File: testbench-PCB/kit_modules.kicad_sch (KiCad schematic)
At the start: 7 parts, among them U2 Rotary_encoder_switch_module, U3 Thermistor_module, U4 Relay_module, U6 Matrix_keyboard, U7 RTC_EEPROM_module

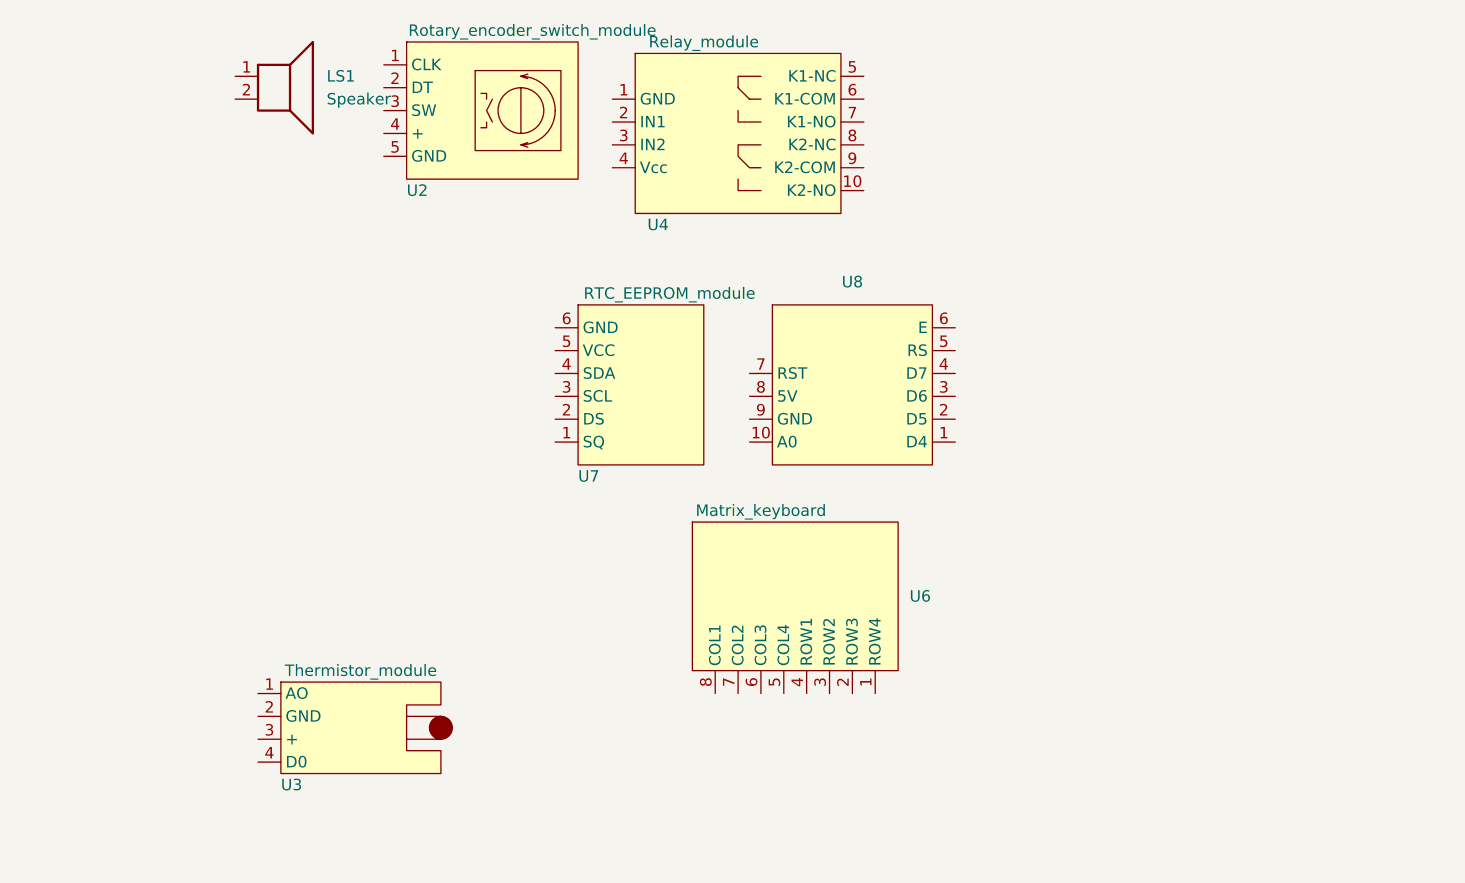
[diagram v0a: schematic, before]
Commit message: Changed USB interface name, MCU moved to separate sheet.
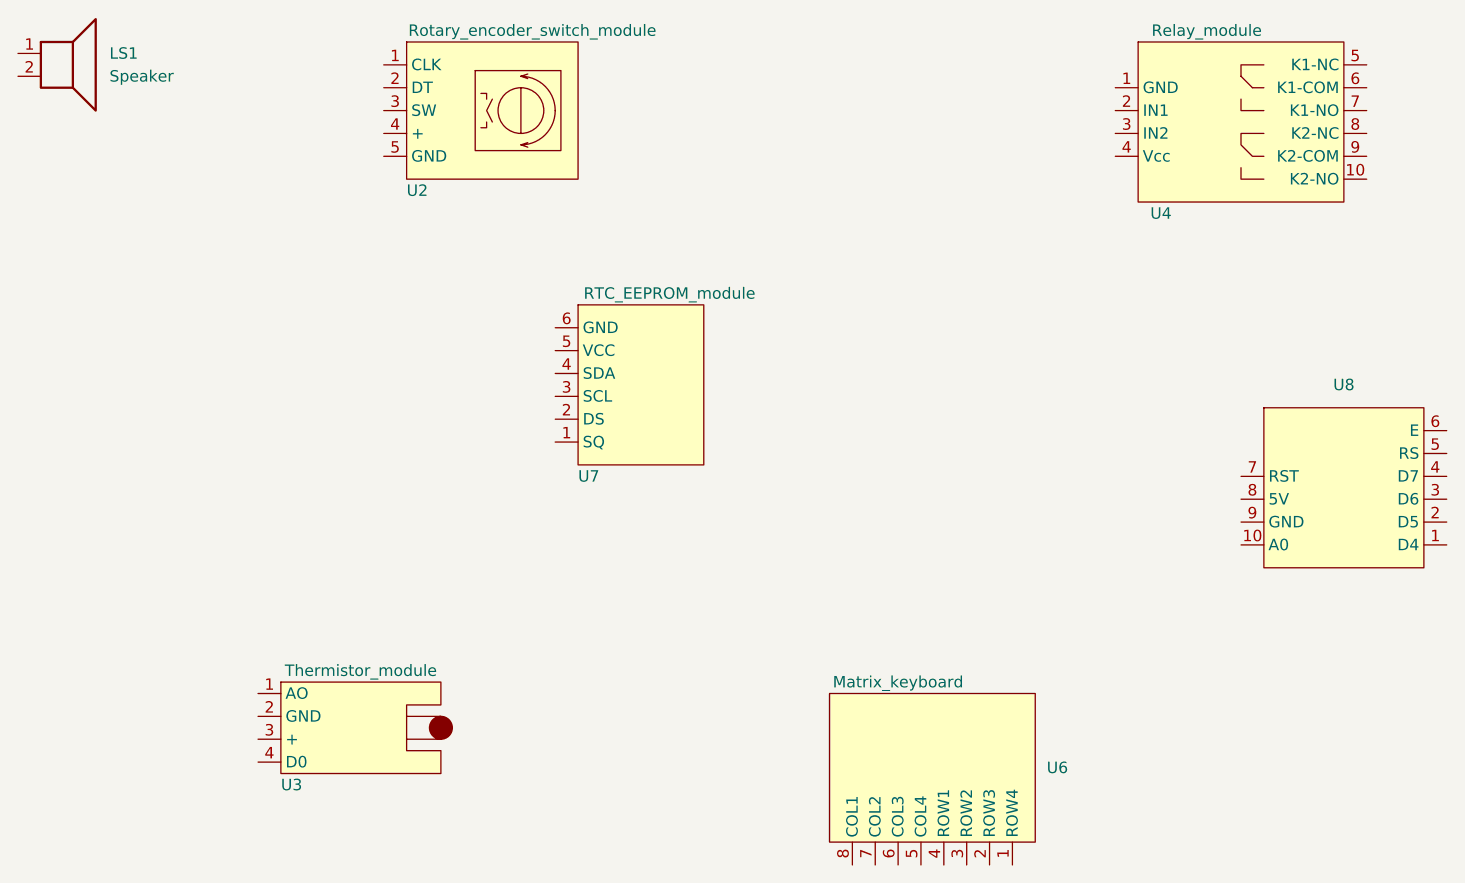
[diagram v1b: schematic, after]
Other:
- moved on the sheet: LS1, U4, U6, U8
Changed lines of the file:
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@@
 (kicad_sch (version 20230121) (generator eeschema)
   (paper "A4")
-  (symbol (lib_id "kit_modules:relay_module") (at 148.59 49.53 0) (unit 1)
-    (in_bom yes) (on_board yes) (dnp no)
-    (property "Reference" "U4" (at 153.67 59.69 0)
-      (effects (font (size 1.27 1.27)))
-    )
-    (property "Value" "Relay_module" (at 158.75 39.37 0)
-      (effects (font (size 1.27 1.27)))
-    )
-    (property "Footprint" "" (at 148.59 53.34 0)
-      (effects (font (size 1.27 1.27)) hide)
-    )
-    (property "Datasheet" "" (at 148.59 53.34 0)
+  (symbol (lib_id "kit_modules:relay_module") (at 204.47 48.26 0) (unit 1)
+    (in_bom yes) (on_board yes) (dnp no)
+    (property "Reference" "U4" (at 209.55 58.42 0)
+      (effects (font (size 1.27 1.27)))
+    )
+    (property "Value" "Relay_module" (at 214.63 38.1 0)
+      (effects (font (size 1.27 1.27)))
+    )
+    (property "Footprint" "" (at 204.47 52.07 0)
+      (effects (font (size 1.27 1.27)) hide)
+    )
+    (property "Datasheet" "" (at 204.47 52.07 0)
       (effects (font (size 1.27 1.27)) hide)
     )
@@
     )
   )
-  (symbol (lib_id "kit_modules:LCD_module") (at 163.83 86.36 0) (unit 1)
+  (symbol (lib_id "kit_modules:LCD_module") (at 218.44 97.79 0) (unit 1)
     (in_bom yes) (on_board yes) (dnp no) (fields_autoplaced)
-    (property "Reference" "U8" (at 175.26 66.04 0)
-      (effects (font (size 1.27 1.27)))
-    )
-    (property "Value" "~" (at 167.64 87.63 0)
-      (effects (font (size 1.27 1.27)))
-    )
-    (property "Footprint" "" (at 167.64 87.63 0)
-      (effects (font (size 1.27 1.27)) hide)
-    )
-    (property "Datasheet" "" (at 167.64 87.63 0)
+    (property "Reference" "U8" (at 229.87 77.47 0)
+      (effects (font (size 1.27 1.27)))
+    )
+    (property "Value" "~" (at 222.25 99.06 0)
+      (effects (font (size 1.27 1.27)))
+    )
+    (property "Footprint" "" (at 222.25 99.06 0)
+      (effects (font (size 1.27 1.27)) hide)
+    )
+    (property "Datasheet" "" (at 222.25 99.06 0)
       (effects (font (size 1.27 1.27)) hide)
     )
@@
     )
   )
-  (symbol (lib_id "kit_modules:matrix_keyboard") (at 157.48 109.22 0) (unit 1)
-    (in_bom yes) (on_board yes) (dnp no)
-    (property "Reference" "U6" (at 181.61 100.965 0)
-      (effects (font (size 1.27 1.27)) (justify left))
-    )
-    (property "Value" "Matrix_keyboard" (at 165.1 91.44 0)
-      (effects (font (size 1.27 1.27)))
-    )
-    (property "Footprint" "" (at 157.48 109.22 0)
-      (effects (font (size 1.27 1.27)) hide)
-    )
-    (property "Datasheet" "" (at 157.48 109.22 0)
+  (symbol (lib_id "kit_modules:matrix_keyboard") (at 172.72 128.27 0) (unit 1)
+    (in_bom yes) (on_board yes) (dnp no)
+    (property "Reference" "U6" (at 196.85 120.015 0)
+      (effects (font (size 1.27 1.27)) (justify left))
+    )
+    (property "Value" "Matrix_keyboard" (at 180.34 110.49 0)
+      (effects (font (size 1.27 1.27)))
+    )
+    (property "Footprint" "" (at 172.72 128.27 0)
+      (effects (font (size 1.27 1.27)) hide)
+    )
+    (property "Datasheet" "" (at 172.72 128.27 0)
       (effects (font (size 1.27 1.27)) hide)
     )
@@
     )
   )
-  (symbol (lib_id "Device:Speaker") (at 111.76 43.18 0) (unit 1)
+  (symbol (lib_id "Device:Speaker") (at 87.63 40.64 0) (unit 1)
     (in_bom yes) (on_board yes) (dnp no) (fields_autoplaced)
-    (property "Reference" "LS1" (at 116.84 43.18 0)
-      (effects (font (size 1.27 1.27)) (justify left))
-    )
-    (property "Value" "Speaker" (at 116.84 45.72 0)
-      (effects (font (size 1.27 1.27)) (justify left))
-    )
-    (property "Footprint" "" (at 111.76 48.26 0)
-      (effects (font (size 1.27 1.27)) hide)
-    )
-    (property "Datasheet" "~" (at 111.506 44.45 0)
-      (effects (font (size 1.27 1.27)) hide)
-    )
+    (property "Reference" "LS1" (at 92.71 40.64 0)
+      (effects (font (size 1.27 1.27)) (justify left))
+    )
+    (property "Value" "Speaker" (at 92.71 43.18 0)
+      (effects (font (size 1.27 1.27)) (justify left))
+    )
+    (property "Footprint" "" (at 87.63 45.72 0)
+      (effects (font (size 1.27 1.27)) hide)
+    )
+    (property "Datasheet" "~" (at 87.376 41.91 0)
+      (effects (font (size 1.27 1.27)) hide)
+    )

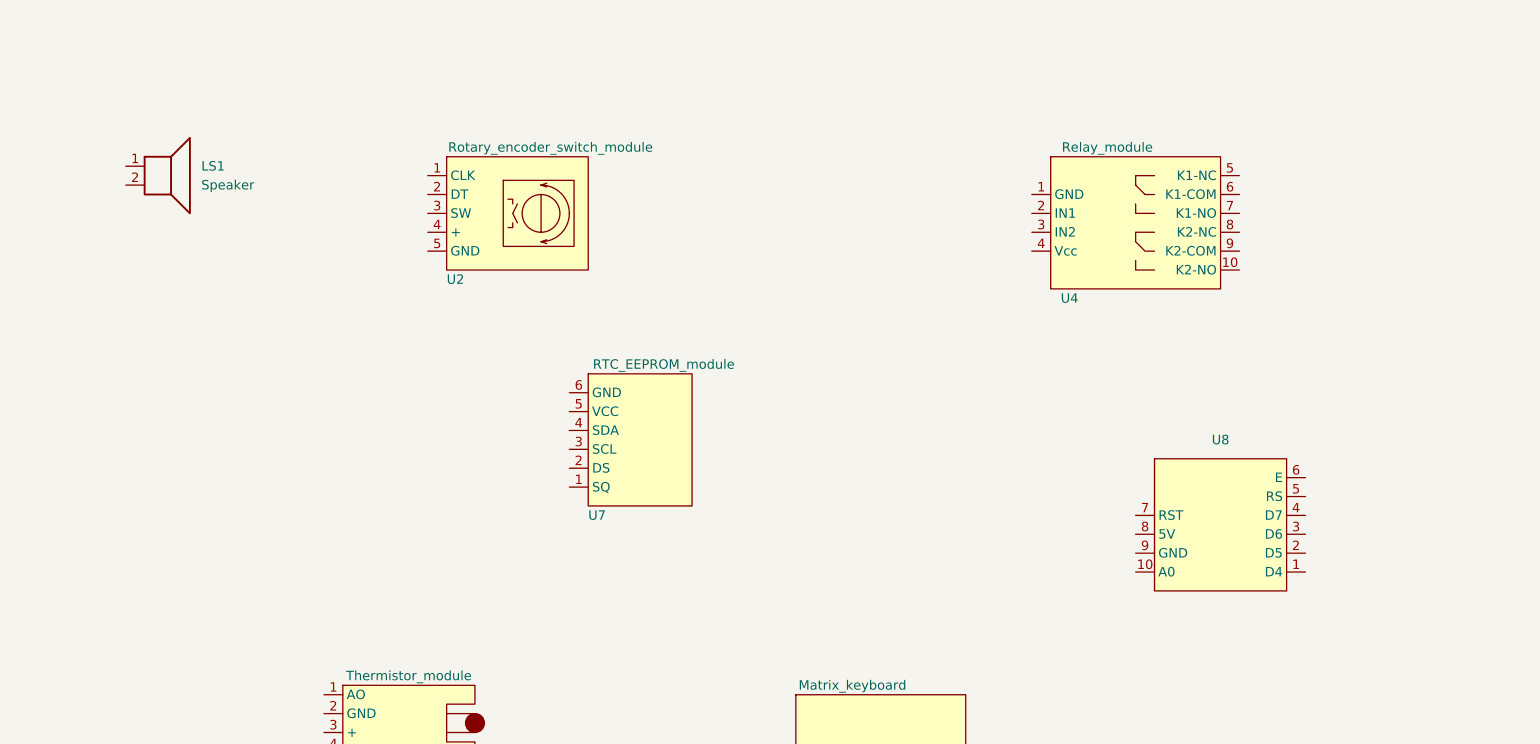
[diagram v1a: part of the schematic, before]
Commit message: Added USB interface.
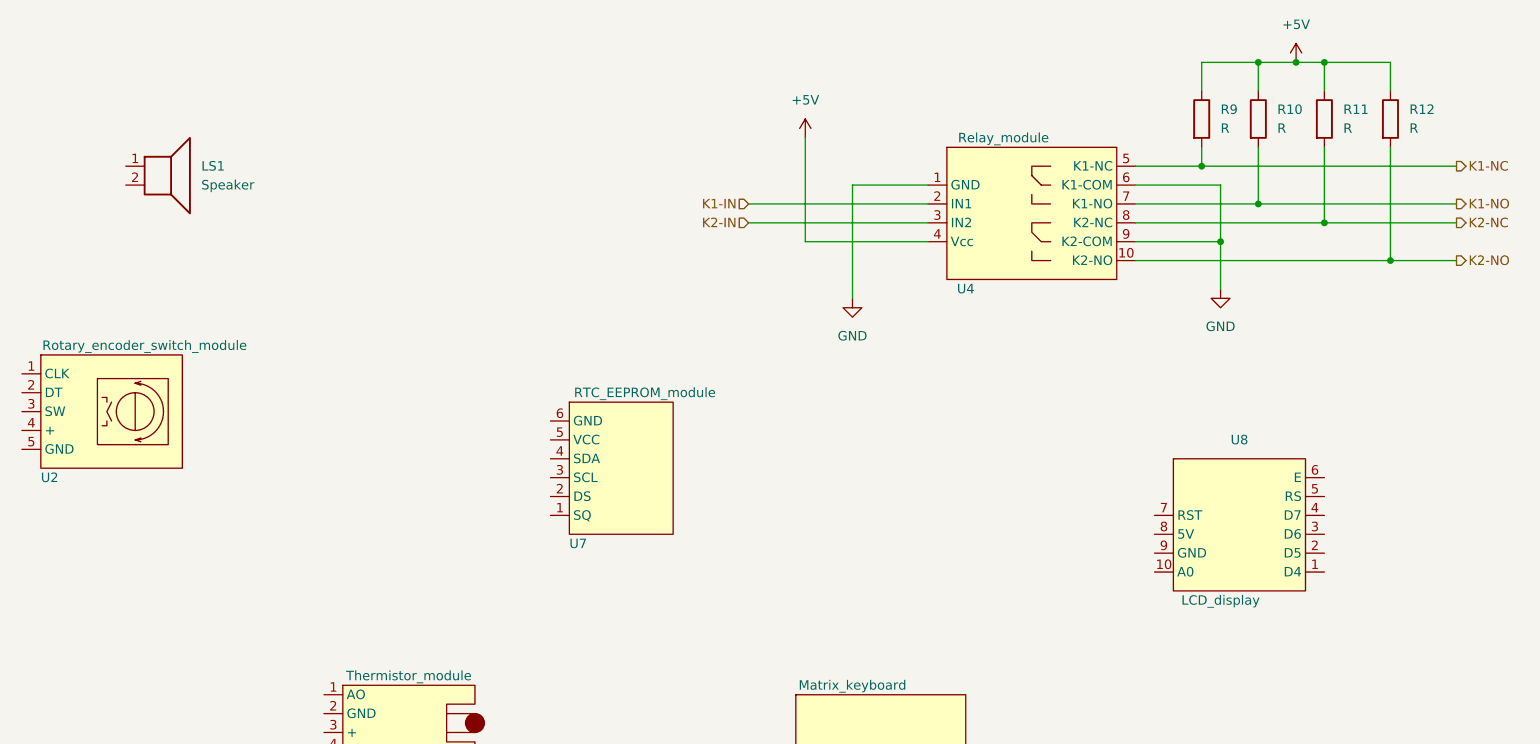
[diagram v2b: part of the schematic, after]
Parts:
- added R10, R11, R12, R9: R, Resistor_SMD:R_0805_2012Metric, symbol Device:R
- U8: value ~ -> LCD_display
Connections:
- net GND: now reaches U4.1 (GND)
- net GND: now also U4.6 (K1-COM), U4.9 (K2-COM)
- net K2-NO: now reaches U4.10 (K2-NO)
- net K2-NO: now also R12.2
- net K1-IN: now reaches U4.2 (IN1)
- net K2-IN: now reaches U4.3 (IN2)
- net +5V: now reaches U4.4 (Vcc)
- net +5V: now also R10.1, R11.1, R12.1, R9.1
- net K1-NC: now reaches U4.5 (K1-NC)
- net K1-NC: now also R9.2
- net K1-NO: now reaches U4.7 (K1-NO)
- net K1-NO: now also R10.2
- net K2-NC: now reaches U4.8 (K2-NC)
- net K2-NC: now also R11.2
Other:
- moved on the sheet: U2, U4, U7, U8

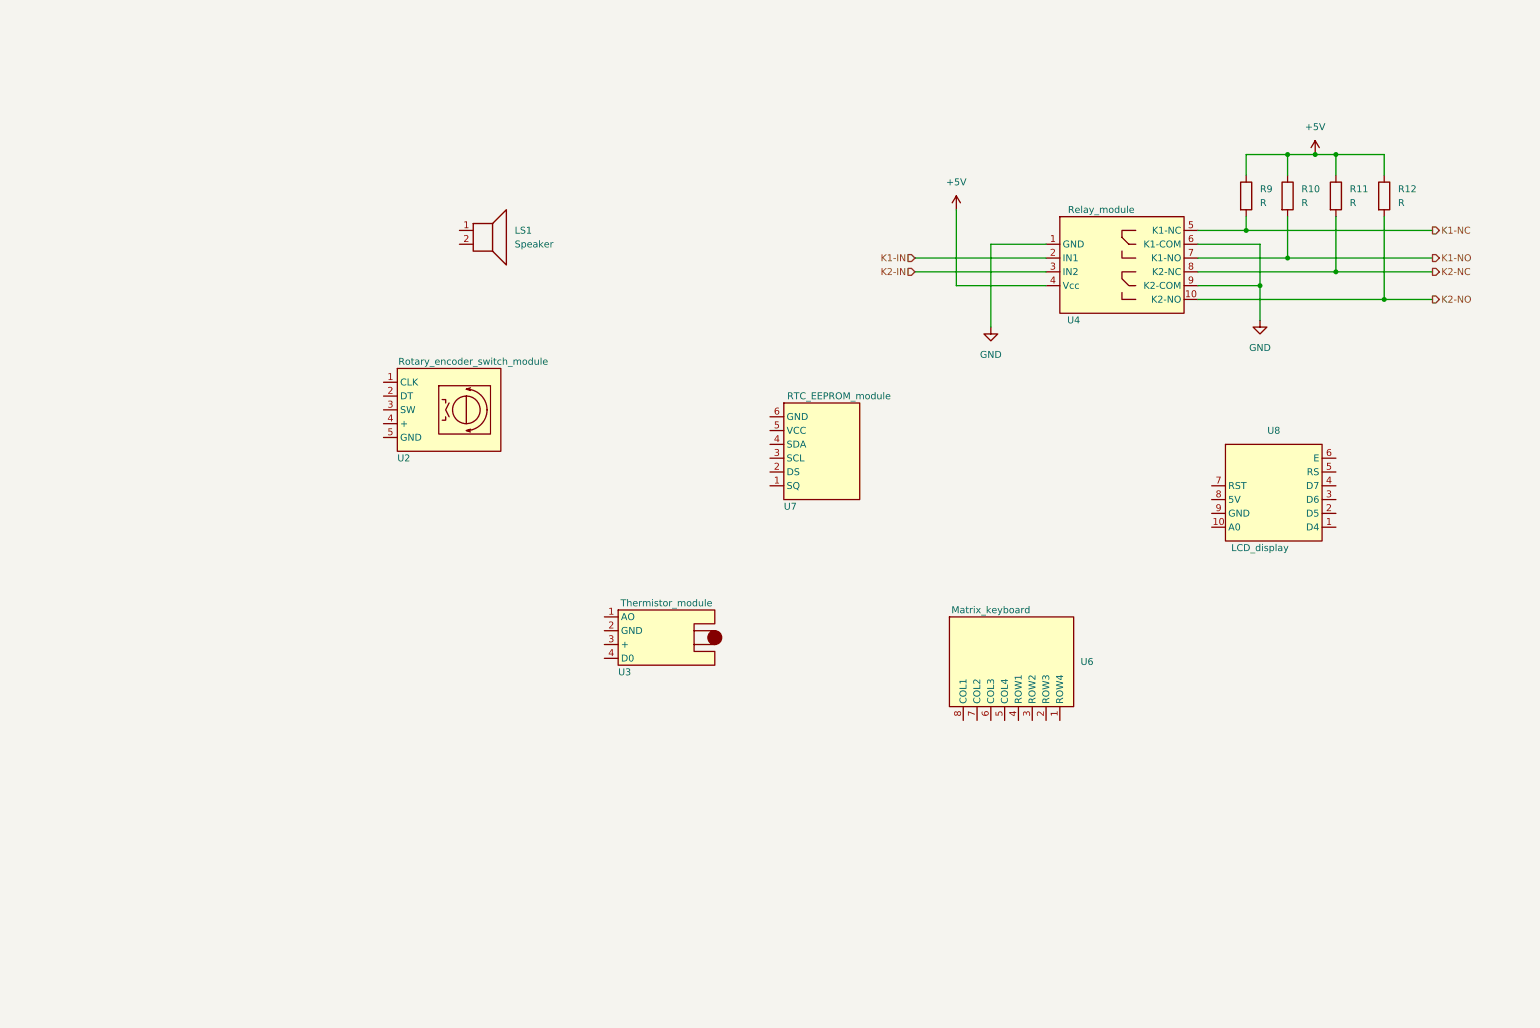
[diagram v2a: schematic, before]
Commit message: Added connection between some modules.
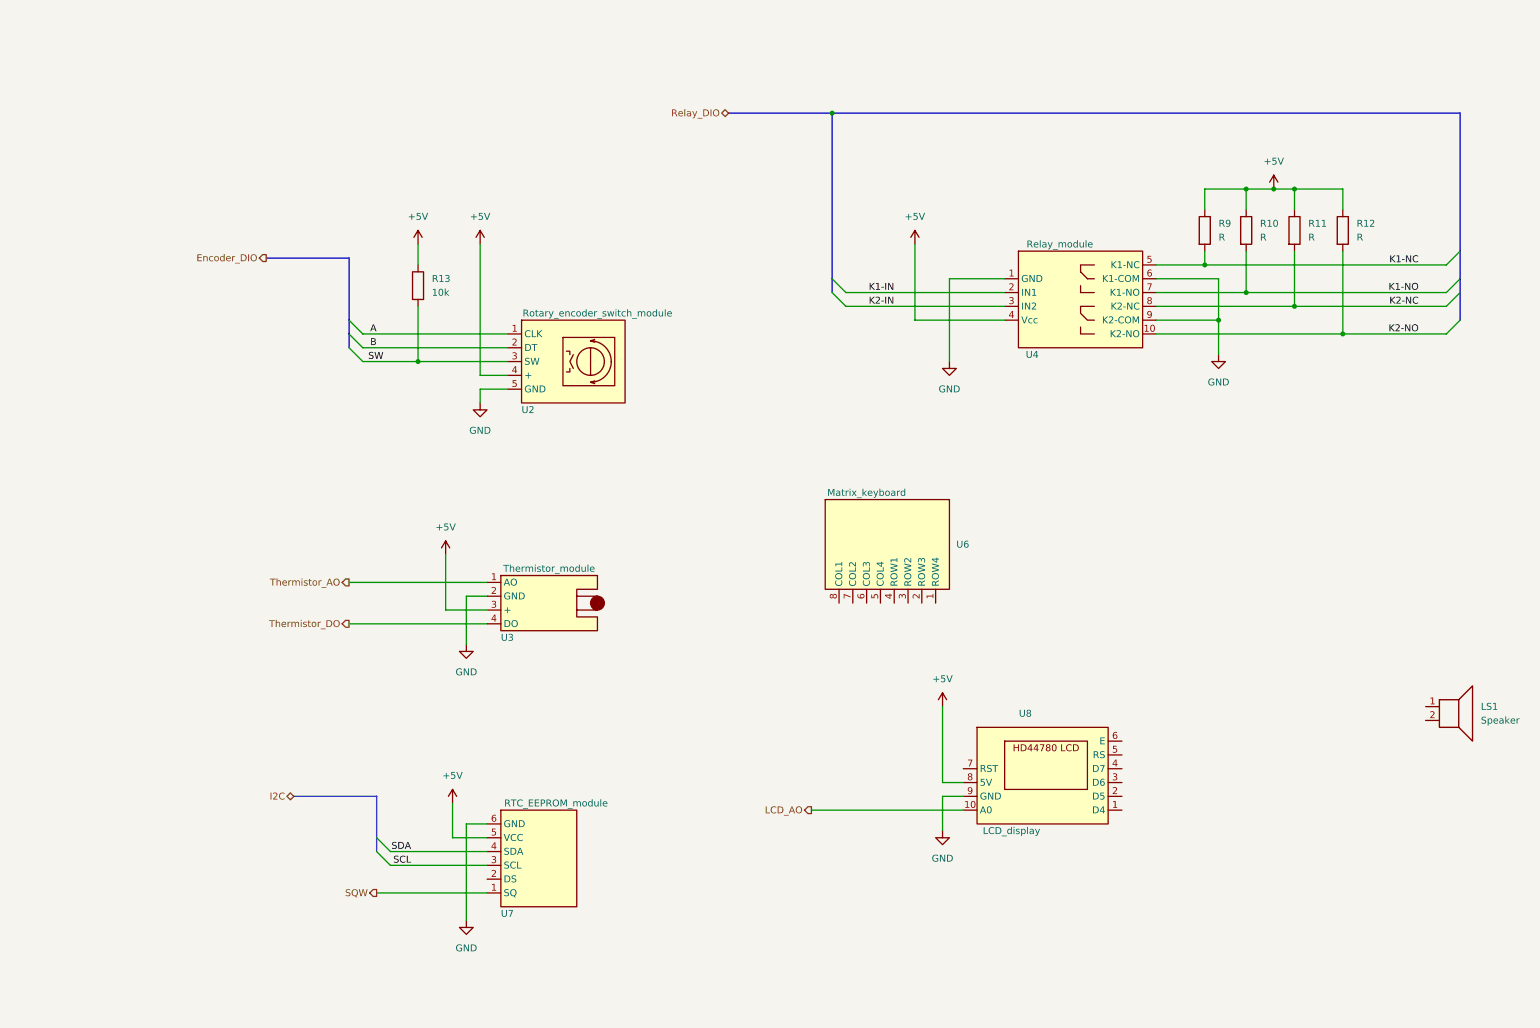
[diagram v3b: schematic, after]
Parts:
- added R13: 10k, Resistor_SMD:R_0805_2012Metric, symbol Device:R
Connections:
- net +5V: now also U2.4 (+), U3.3 (+), U7.5 (VCC), U8.8 (5V), R13.1
- net GND: now also U2.5 (GND), U3.2 (GND), U7.6 (GND), U8.9 (GND)
- net LCD_AO: now reaches U8.10 (A0)
- net Thermistor_AO: now reaches U3.1 (AO)
- net Thermistor_DO: now reaches U3.4 (DO)
- net A: now reaches U2.1 (CLK)
- net B: now reaches U2.2 (DT)
- net SW: now reaches U2.3 (SW)
- net SW: now also R13.2
- net SQW: now reaches U7.1 (SQ)
- net SCL: now reaches U7.3 (SCL)
- net SDA: now reaches U7.4 (SDA)
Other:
- moved on the sheet: LS1, R10, R11, R12, R9, U2, U3, U4, U6, U7
